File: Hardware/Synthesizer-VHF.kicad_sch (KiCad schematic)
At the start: 87 parts, among them J1 Screw_Terminal_01x02, J2 Scope, J3 REF Select, J4 USB-C 2.0 16P, J5 REF_IN, J6 Scope, J7 RFOUTA, J8 Header 1x3, J9 RFOUTB, U1 LM7805A, U2 FT231XQ, U3 ATtiny1616-M, U4 ADF4350, U5 GM1200ACPZ, U6 GM1200ACPZ, X1 IQXO-70

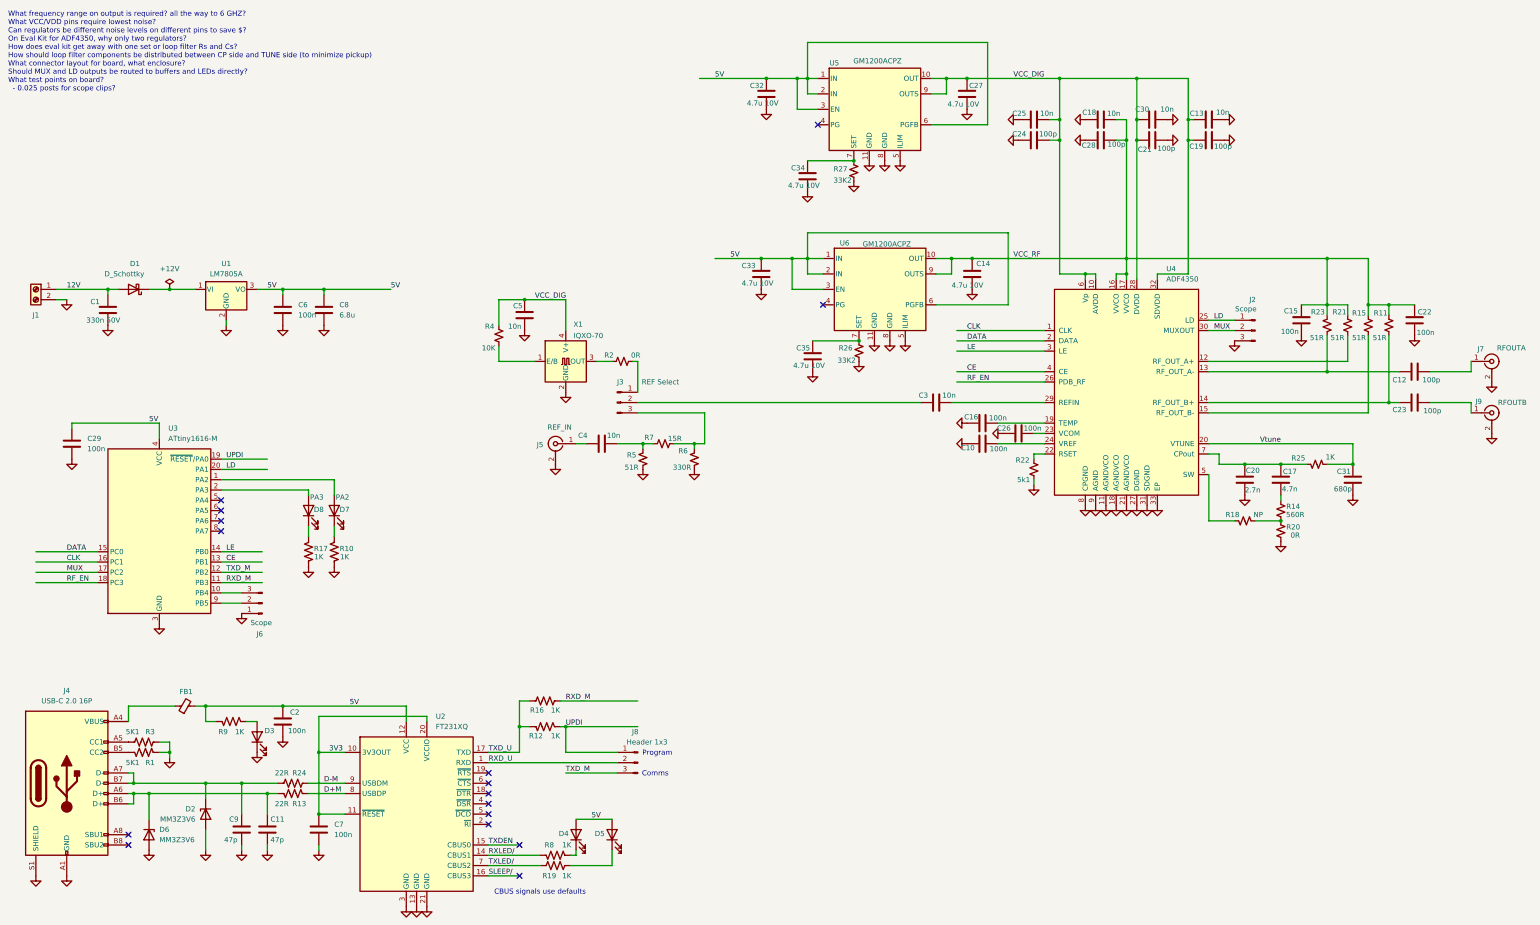
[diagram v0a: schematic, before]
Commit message: Final version for costing and possible ordering Change TCXO to on available from LCSC
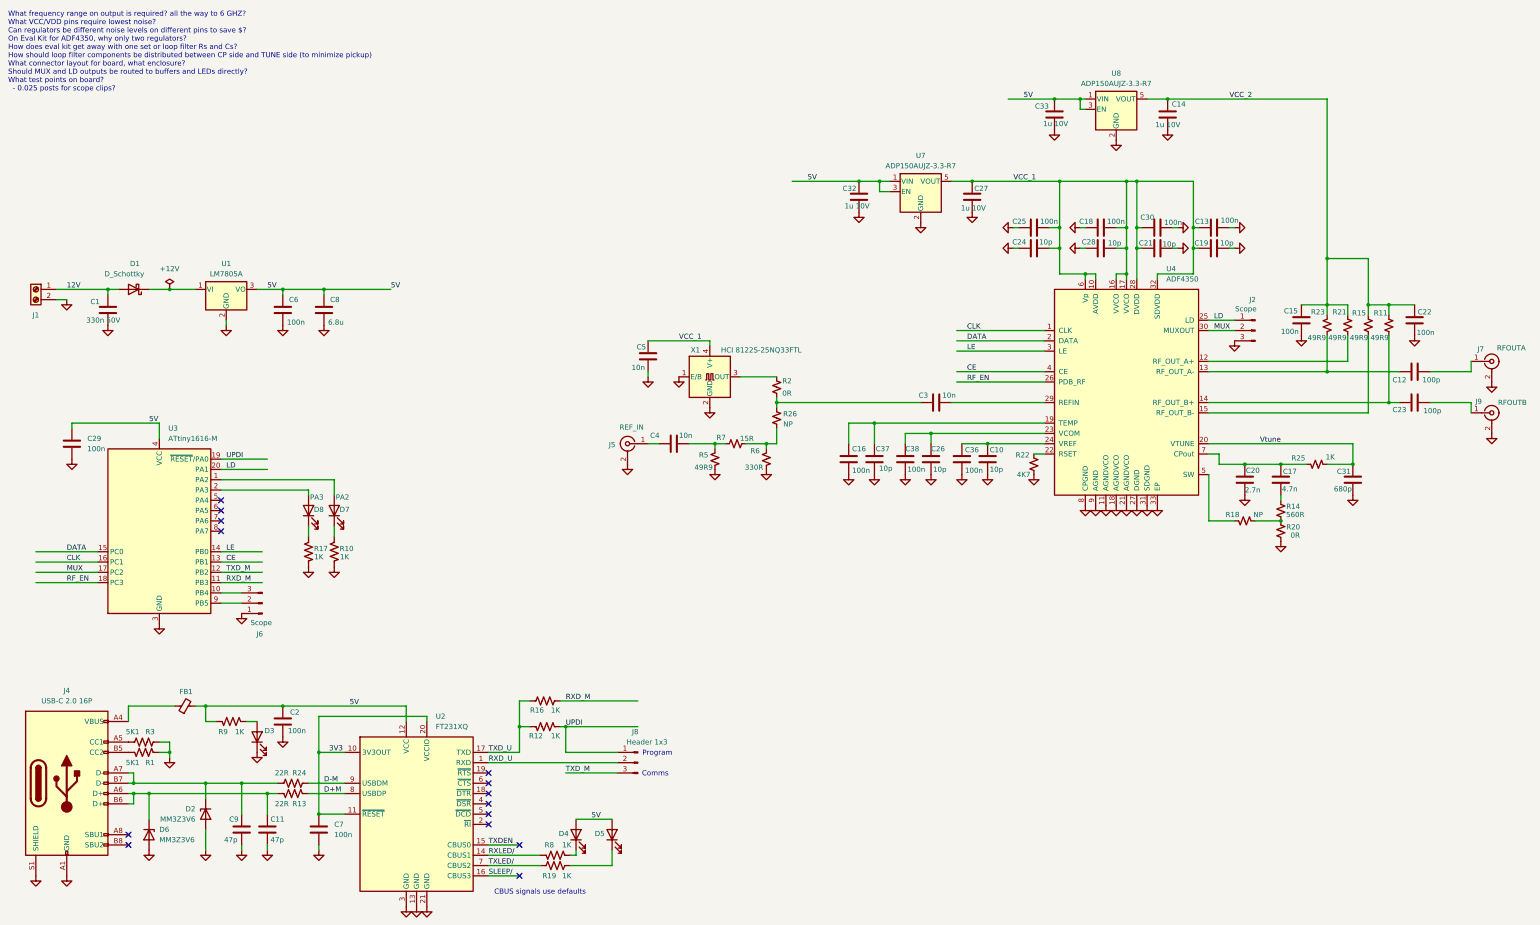
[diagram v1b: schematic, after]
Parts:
- removed C34, C35: 4.7u 10V, Synthesizer:Cap_0402, symbol Device:C
- removed J3: REF Select, Connector_PinHeader_2.54mm:PinHeader_1x03_P2.54mm_Vertical, symbol Connector:Conn_01x03_Pin
- removed R27: 33K2, Synthesizer:Res_0402, symbol Device:R_Small_US
- removed R4: 10K, Synthesizer:Res_0402, symbol Device:R_Small_US
- removed U5, U6: GM1200ACPZ, Package_DFN_QFN:DFN-10-1EP_3x3mm_P0.5mm_EP1.65x2.38mm_ThermalVias, symbol Synthesizer:GM1200ACPZ
- added C36, C38: 100n, Synthesizer:Cap_0402, symbol Device:C
- added C37: 10p, Synthesizer:Cap_0402, symbol Device:C
- added U7, U8: ADP150AUJZ-3.3-R7, Package_TO_SOT_SMD:SOT-23-5, symbol Synthesizer:ADP150AUJZ-3.3-R7
- C10, C26: value 100n -> 10p
- C13, C18, C25, C30: value 10n -> 100n
- C14, C27, C32, C33: value 4.7u 10V -> 1u 10V
- C19, C21, C24, C28: value 100p -> 10p
- R11, R15, R21, R23, R5: value 51R -> 49R9
- R2: footprint Synthesizer:Res_0402 -> Resistor_SMD:R_0805_2012Metric
- R22: value 5k1 -> 4K7; LCSC C144745 -> (none)
- R26: value 33K2 -> NP; footprint Synthesizer:Res_0402 -> Resistor_SMD:R_0805_2012Metric; LCSC C25744 -> C17168
- X1: value IQXO-70 -> HCI 8122S-25NQ33FTL; footprint Synthesizer:Oscillator_SMD_IQD_IQXO70-4Pin_7.5x5.0mm -> Synthesizer:Oscillator_SMD2520
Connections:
- net 5V: now also U7.1 (VIN), U7.3 (EN), U8.1 (VIN), U8.3 (EN)
- net GND: now also X1.1 (E/B), C36.2, C37.1, C38.2, U7.2 (GND), U8.2 (GND); no longer R26.1
- net at R26.2: now also R6.1, R7.2
- net at C16.2, U4.19 (TEMP): now also C37.2
- net at C26.1, U4.23 (VCOM): now also C38.1
- net at C10.1, U4.24 (VREF): now also C36.1
- net at R2.2: now also C3.2, R26.1
- net VCC_DIG renamed VCC_1
- net VCC_1: now also C18.1, C28.2, U4.16 (VVCO), U4.17 (VVCO), U7.5 (VOUT)
- net VCC_RF renamed VCC_2
- net VCC_2: now also U8.5 (VOUT); no longer C18.1, C28.2, U4.16 (VVCO), U4.17 (VVCO)
- no-connect marks 16 -> 14
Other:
- moved on the sheet: C10, C13, C14, C16, C18, C19, C21, C24, C25, C26, C27, C28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

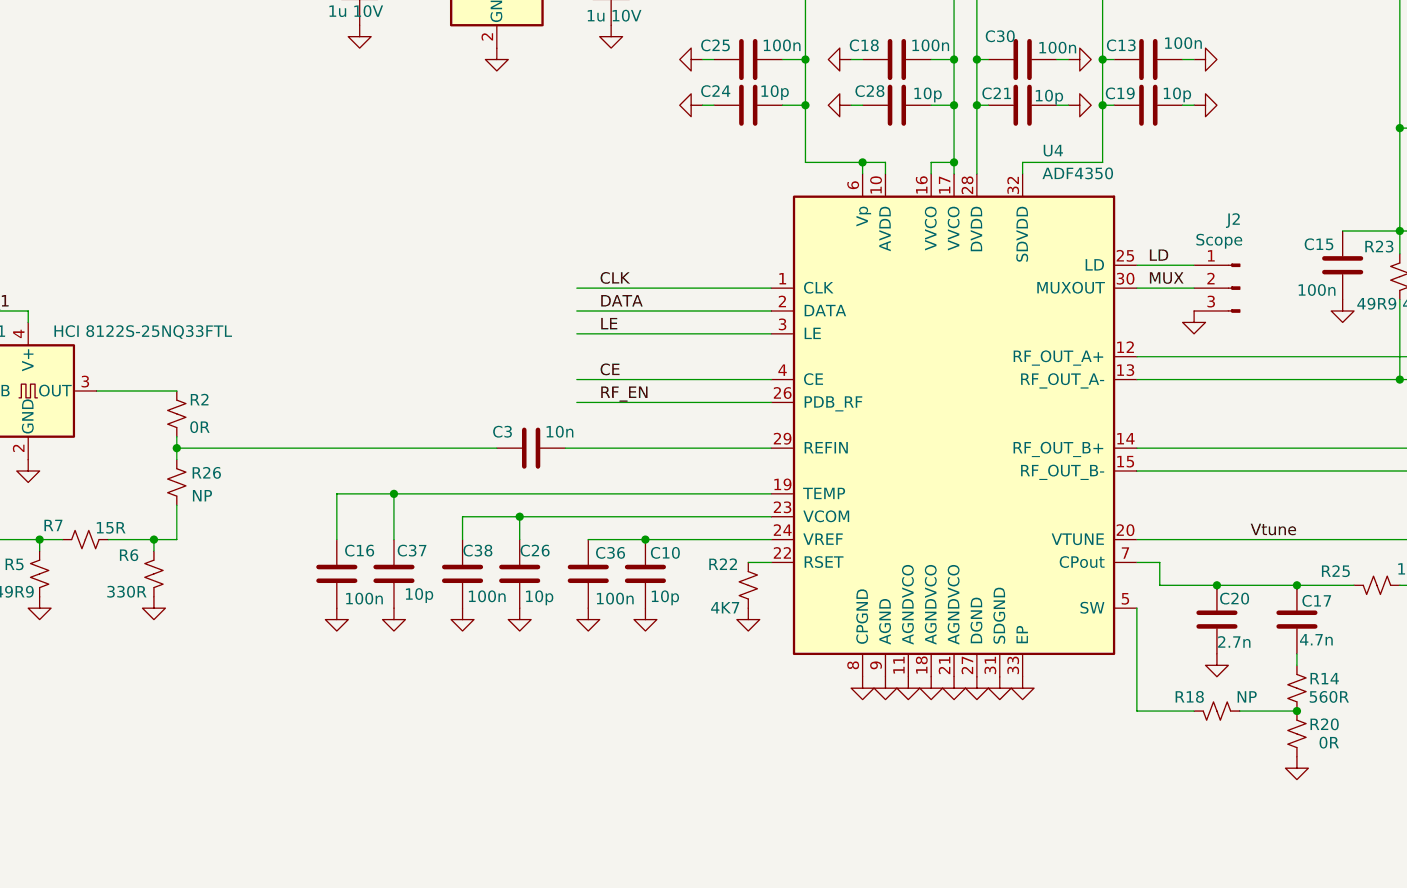
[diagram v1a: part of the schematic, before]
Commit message: This what got sent to fab.  The wiring for SPI between MCU and ADF4351 is not connected to the hardware SPI pins and will need bit banging.
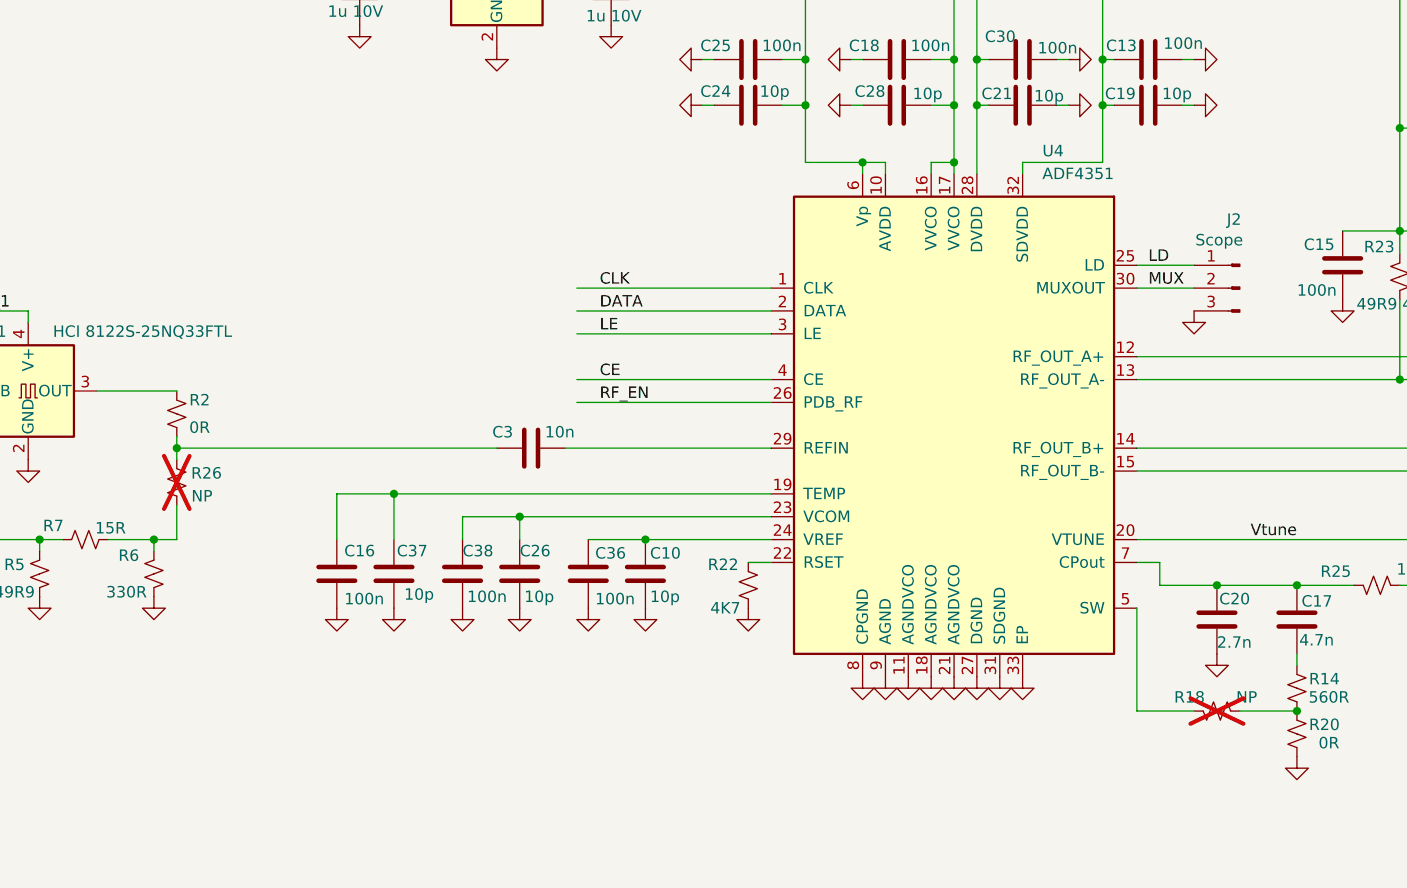
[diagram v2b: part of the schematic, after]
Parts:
- C1: LCSC (none) -> C282682
- C10: LCSC C15195 -> C32949
- C11, C9: LCSC C1671 -> C1567
- C12, C23: LCSC C32949 -> C1546
- C13, C18, C22, C25, C30, C36: LCSC C15195 -> C1525
- C14, C27, C33: LCSC C12530 -> C52923
- C2, C29, C6, C7: LCSC C14663 -> C1525
- C26, C37: LCSC C1525 -> C32949
- C32: LCSC (none) -> C52923
- D2, D6: LCSC C116949 -> C22395574
- D3: value White -> blue; LCSC C2290 -> C364550
- D4, D5: LCSC C72038 -> C434449
- D7, D8: LCSC C2290 -> C364550
- R1, R3: LCSC C23186 -> C105872
- R10, R12, R16, R17, R19, R8, R9: LCSC C21190 -> C11702
- R13, R24: LCSC C23345 -> C93929
- R18, R26: now not fitted; now left out of the parts list
- R20: LCSC C17477 -> C17168
- R22: LCSC (none) -> C105871
- U4: value ADF4350 -> ADF4351; LCSC C98705 -> C654681
- U7, U8: LCSC (none) -> C29149
- X1: LCSC (none) -> C20623084
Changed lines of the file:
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@@
 			)
 		)
-		(property "LCSC" "C2290"
+		(property "LCSC" "C364550"
 			(at 158.75 289.56 0)
 			(effects
@@
 			)
 		)
+		(property "LCSC" "C20623084"
+			(at 184.404 120.396 0)
+			(effects
+				(font
+					(size 1.27 1.27)
+				)
+				(hide yes)
+			)
+		)
 		(pin "2"
 		)
@@
 			)
 		)
-		(property "LCSC" "C15195"
+		(property "LCSC" "C1525"
 			(at 196.85 -194.31 0)
 			(effects
@@
 			)
 		)
+		(property "LCSC" "C29149"
+			(at 288.29 52.07 0)
+			(effects
+				(font
+					(size 1.27 1.27)
+				)
+				(hide yes)
+			)
+		)
 		(pin "5"
 		)
@@
 		(unit 1)
 		(exclude_from_sim no)
-		(in_bom yes)
+		(in_bom no)
 		(on_board yes)
-		(dnp no)
+		(dnp yes)
 		(property "Reference" "R18"
 			(at 316.992 161.036 90)
@@
 			)
 		)
-		(property "LCSC" "C32949"
+		(property "LCSC" "C1546"
 			(at 487.68 -236.22 0)
 			(effects
@@
 			)
 		)
-		(property "LCSC" ""
+		(property "LCSC" "C105871"
 			(at 532.13 2.54 0)
 			(effects
@@
 			)
 		)
-		(property "LCSC" ""
+		(property "LCSC" "C282682"
 			(at 1.27 139.7 0)
 			(effects
@@
 			)
 		)
-		(property "LCSC" "C21190"
+		(property "LCSC" "C11702"
 			(at 91.948 169.418 0)
 			(effects
@@
 			)
 		)
-		(property "LCSC" "C1671"
+		(property "LCSC" "C1567"
 			(at -6.35 386.08 0)
 			(effects
@@
 			)
 		)
-		(property "LCSC" "C23186"
+		(property "LCSC" "C105872"
 			(at -80.01 269.24 0)
 			(effects
@@
 			)
 		)
-		(property "LCSC" "C14663"
+		(property "LCSC" "C1525"
 			(at -6.35 386.08 0)
 			(effects
@@
 			)
 		)
-		(property "LCSC" "C15195"
+		(property "LCSC" "C1525"
 			(at -5.08 290.83 0)
 			(effects
@@
 			)
 		)
+		(property "LCSC" "C29149"
+			(at 240.03 72.39 0)
+			(effects
+				(font
+					(size 1.27 1.27)
+				)
+				(hide yes)
+			)
+		)
 		(pin "5"
 		)
@@
 			)
 		)
-		(property "LCSC" "C21190"
+		(property "LCSC" "C11702"
 			(at 67.818 214.63 0)
 			(effects
@@
 			)
 		)
-		(property "LCSC" "C14663"
+		(property "LCSC" "C1525"
 			(at 16.51 139.7 0)
 			(effects
@@
 			)
 		)
-		(property "LCSC" "C21190"
+		(property "LCSC" "C11702"
 			(at 98.298 169.418 0)
 			(effects
@@
 			)
 		)
-		(property "LCSC" "C23186"
+		(property "LCSC" "C105872"
 			(at -77.47 167.64 0)
 			(effects
@@
 		(unit 1)
 		(exclude_from_sim no)
-		(in_bom yes)
+		(in_bom no)
 		(on_board yes)
-		(dnp no)
+		(dnp yes)
 		(property "Reference" "R26"
 			(at 207.772 136.144 0)
@@
 			)
 		)
-		(property "LCSC" "C12530"
+		(property "LCSC" "C52923"
 			(at 48.26 163.83 0)
 			(effects
@@
 			)
 		)
-		(property "LCSC" "C17477"
+		(property "LCSC" "C17168"
 			(at 0 330.2 0)
 			(effects
@@
 			)
 		)
-		(property "LCSC" "C21190"
+		(property "LCSC" "C11702"
 			(at 148.336 250.19 0)
 			(effects
@@
 			)
 		)
-		(property "LCSC" "C15195"
+		(property "LCSC" "C1525"
 			(at 400.05 401.32 0)
 			(effects
@@
 			)
 		)
-		(property "LCSC" ""
+		(property "LCSC" "C52923"
 			(at 3.81 163.83 0)
 			(effects
@@
 			)
 		)
-		(property "LCSC" "C12530"
+		(property "LCSC" "C52923"
 			(at 54.61 163.83 0)
 			(effects
@@
 			)
 		)
-		(property "LCSC" "C23345"
+		(property "LCSC" "C93929"
 			(at -50.8 135.89 0)
 			(effects
@@
 			)
 		)
-		(property "Value" "ADF4350"
+		(property "Value" "ADF4351"
 			(at 300.6441 102.87 0)
 			(effects
@@
 			)
 		)
-		(property "Datasheet" "https://www.analog.com/media/en/technical-documentation/data-sheets/ADF4350.pdf"
+		(property "Datasheet" "https://www.analog.com/media/en/technical-documentation/data-sheets/ADF4351.pdf"
 			(at 299.72 172.466 0)
 			(effects
@@
 			)
 		)
-		(property "Description" "137.5-4400MHz fractional-N PLL, LFCSP-32"
+		(property "Description" "Wideband Synthesizerwith Integrated VCO"
 			(at 291.338 180.086 0)
 			(effects
@@
 			)
 		)
-		(property "LCSC" "C98705"
+		(property "LCSC" "C654681"
 			(at 0 261.62 0)
 			(effects
@@
 			)
 		)
-		(property "LCSC" "C2290"
+		(property "LCSC" "C364550"
 			(at 165.1 289.56 0)
 			(effects
@@
 			)
 		)
-		(property "LCSC" "C1525"
+		(property "LCSC" "C32949"
 			(at 483.87 8.89 0)
 			(effects
@@
 			)
 		)
-		(property "LCSC" "C1671"
+		(property "LCSC" "C1567"
 			(at 151.13 386.08 0)
 			(effects
@@
 			)
 		)
-		(property "LCSC" "C72038"
+		(property "LCSC" "C434449"
 			(at 293.37 401.32 0)
 			(effects
@@
 			)
 		)
-		(property "LCSC" "C1525"
+		(property "LCSC" "C32949"
 			(at -21.59 288.29 0)
 			(effects
@@
 			)
 		)
-		(property "LCSC" "C21190"
+		(property "LCSC" "C11702"
 			(at 145.034 215.646 0)
 			(effects
@@
 			)
 		)
-		(property "Value" "White"
+		(property "Value" "blue"
 			(at 80.518 215.9 90)
 			(effects
@@
 			)
 		)
-		(property "LCSC" "C2290"
+		(property "LCSC" "C364550"
 			(at 200.66 281.94 0)
 			(effects
@@
 			)
 		)
-		(property "LCSC" "C21190"
+		(property "LCSC" "C11702"
 			(at 145.288 209.296 0)
 			(effects
@@
 			)
 		)
-		(property "LCSC" "C32949"
+		(property "LCSC" "C1546"
 			(at 495.3 -228.6 0)
 			(effects
@@
 			)
 		)
-		(property "LCSC" "C116949"
+		(property "LCSC" "C22395574"
 			(at -99.06 189.23 0)
 			(effects
@@
 			)
 		)
-		(property "LCSC" "C116949"
+		(property "LCSC" "C22395574"
 			(at 207.01 166.37 0)
 			(effects
@@
 			)
 		)
-		(property "LCSC" "C72038"
+		(property "LCSC" "C434449"
 			(at 302.26 410.21 0)
 			(effects
@@
 			)
 		)
-		(property "LCSC" "C15195"
+		(property "LCSC" "C1525"
 			(at 10.16 226.06 0)
 			(effects
@@
 			)
 		)
-		(property "LCSC" "C23345"
+		(property "LCSC" "C93929"
 			(at -53.34 321.31 0)
 			(effects
@@
 			)
 		)
-		(property "LCSC" "C14663"
+		(property "LCSC" "C1525"
 			(at 2.54 201.93 0)
 			(effects
@@
 			)
 		)
-		(property "LCSC" "C12530"
+		(property "LCSC" "C52923"
 			(at 1.27 163.83 0)
 			(effects
@@
 			)
 		)
-		(property "LCSC" "C15195"
+		(property "LCSC" "C1525"
 			(at 386.08 387.35 0)
 			(effects
@@
 			)
 		)
-		(property "LCSC" "C21190"
+		(property "LCSC" "C11702"
 			(at 148.336 242.57 0)
 			(effects
@@
 			)
 		)
-		(property "LCSC" "C14663"
+		(property "LCSC" "C1525"
 			(at -2.54 337.82 0)
 			(effects
@@
 			)
 		)
-		(property "LCSC" "C15195"
+		(property "LCSC" "C1525"
 			(at 180.34 -177.8 0)
 			(effects
@@
 			)
 		)
-		(property "LCSC" "C15195"
+		(property "LCSC" "C32949"
 			(at 1.27 290.83 0)
 			(effects
